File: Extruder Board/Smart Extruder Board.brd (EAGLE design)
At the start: 36 x 30 mm, 17 parts

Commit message: BCN3D Electronics REV.E tested and manufactured
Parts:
- removed FFC1: FFC_20V_90G_1MM", MarcEagleParts:SAMTEC_ZF1-T-WT
- removed HALL: (no value), adafruit:JSTPH3
- removed HOTEND: (no value), MarcEagleParts:JSTPH3
- removed TP1, TP2, TP3, TP4, TP7: TPB1,27, testpad:B1,27
- added CN1: (no value), MarcEagleParts:JST_PA_04
- added ENDSTOP: (no value), SparkFun-Connectors:JST-2-SMD
- added U$6: (no value), MarcEagleParts:FCIM_LOGO
- added VERT_FFC1: FFC_20V_90G_1MM3, MarcEagleParts:FCI_20WAY_1MM_3ST
- moved U$3 25.0 mm to (1.50, 24.5)
- moved TP6 24.0 mm to (30.8, 23.9), flipped to the top, turned to 270 degrees
- moved TP5 12.3 mm to (7.01, 18.9), flipped to the top
- moved U$4 9.77 mm to (22.1, 4.47)
- moved U$2 5.71 mm to (24.0, 3.00)
- moved U$5 4.88 mm to (7.72, 6.78)
- moved U$1 4.67 mm to (31.0, 28.0)
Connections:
- removed net ATLVL: FFC1.20, HALL.2, TP4.TP
- new net GNDTHERM: CN1.4, VERT_FFC1.2
- new net Z-ENDSTOP: ENDSTOP.2, VERT_FFC1.20
- net +24V: now also CN1.1, VERT_FFC1.10, VERT_FFC1.12, VERT_FFC1.18, VERT_FFC1.19, VERT_FFC1.8; no longer FFC1.10, FFC1.12, FFC1.18, FFC1.19, FFC1.8, HOTEND.1
- net +5V: now also VERT_FFC1.1; no longer FFC1.1, HALL.3
- net GND: now also ENDSTOP.1, VERT_FFC1.11, VERT_FFC1.17, VERT_FFC1.4, VERT_FFC1.7, VERT_FFC1.9, VERT_FFC1.GND1, VERT_FFC1.GND2; no longer FFC1.11, FFC1.17, FFC1.2, FFC1.4, FFC1.7, FFC1.9, FFC1.GND1, FFC1.GND2, HALL.1, HOTEND.4, TP7.TP
- net HOTEND: now also CN1.2, VERT_FFC1.13, VERT_FFC1.14, VERT_FFC1.15, VERT_FFC1.16; no longer FFC1.13, FFC1.14, FFC1.15, FFC1.16, HOTEND.2, TP3.TP
- net HOTEND_THERM: now also CN1.3, VERT_FFC1.3; no longer FFC1.3, HOTEND.3, TP1.TP
- net LFAN: now also VERT_FFC1.5, VERT_FFC1.6; no longer FFC1.5, FFC1.6, TP2.TP
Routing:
- net Z-ENDSTOP: track 0.00 -> 43.1 mm
- net +5V: track 38.1 -> 4.72 mm, vias 1 -> 0
- net ATLVL: track 23.1 -> 0.00 mm, vias 2 -> 0
- net GNDTHERM: track 0.00 -> 22.5 mm
- net +24V: track 25.4 -> 8.94 mm, vias 1 -> 0
- net HOTEND_THERM: track 16.4 -> 19.7 mm, vias 2 -> 0
- net HOTEND: track 2.40 -> 0.00 mm, vias 1 -> 8
- net LFAN: track 30.5 -> 32.5 mm
- added copper zone on layer 16, net HOTEND
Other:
- board size 36 x 30 mm -> 33 x 30 mm
- board text added: "+"
- board text added: "BCN3D Electronics Extruder Board v1.0 Designed in Barcelona ___________________ May 2015 - REV_D"
- board text added: "HOTEND"
- board text added: "THRM"
- board text removed: "BCN3D Electronics çextruder Board v1.0 Designed in Barcelona ___________________ Extruder Board - Jan 2015 Marc Cobler - REV_B ___________________"
- board text removed: "Fundacio CIM"

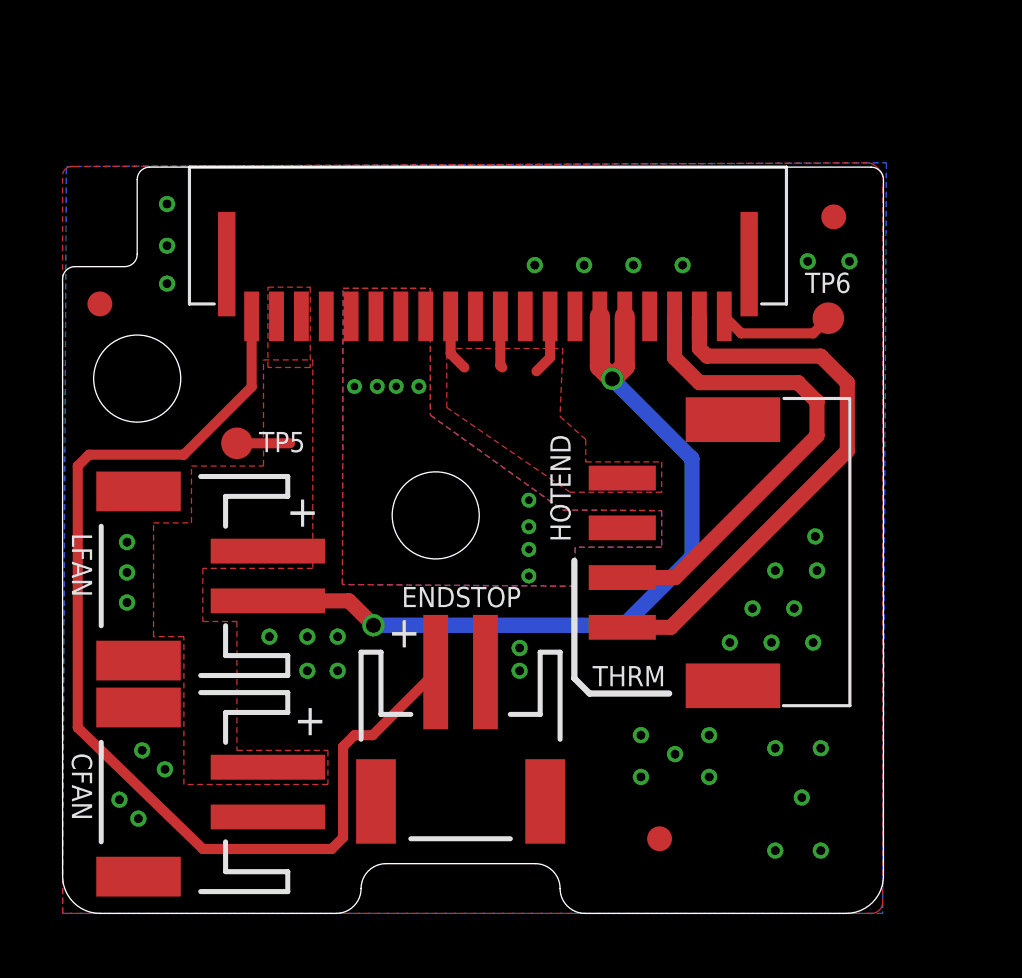
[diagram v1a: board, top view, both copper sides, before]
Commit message: File for the REV.H
Files from the REV.H Released with new and more documentation.
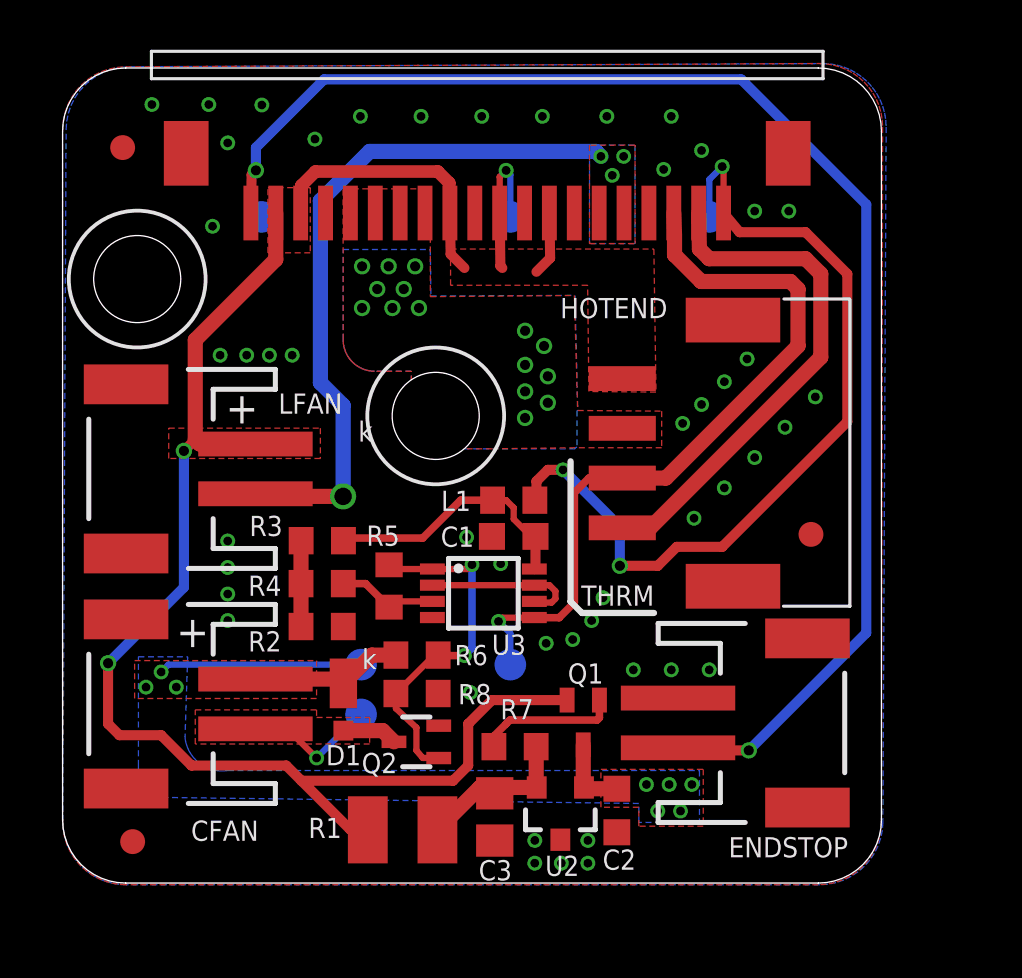
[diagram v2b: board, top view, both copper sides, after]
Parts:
- removed TP5, TP6: TPB1,27, testpad:B1,27
- removed U$4: (no value), MarcEagleParts:CC_LOGO
- added 24V, 5V, CFAN+, CFAN-, GND, THERM: TPB1,27, testpad:B1,27
- added C1, C2: 100n, rcl:C0603K
- added C3: 330n, rcl:C0805
- added D1: PD3S160, diode:POWERDI323
- added L1, R4, R6: 1k, rcl:R0603
- added Q1: BC807W, transistor-pnp:SOT323-BEC
- added Q2: MOSFET-NSOT323, MarcEagleParts:SOT323
- added R1: 100, rcl:R1210
- added R2, R8: 10k, rcl:R0603
- added R3: 5k23, rcl:R0603
- added R5: 200k, rcl:R0603
- added R7: 22.6K, rcl:R0603
- added U2: LM3480IM4, SparkFun-PowerIC:SOT23-3
- added U3: LM392MMSOP8, MarcEagleParts:MSOP8
- VERT_FFC1: value FFC_20V_90G_1MM3 -> 68612014422; device MarcEagleParts:FCI_20WAY_1MM_3ST -> FPC_FFC_Connectors_:68612014422
- moved U$6 22.8 mm to (30.9, -0.50)
- moved U$2 21.2 mm to (2.82, 2.89)
- moved U$1 12.8 mm to (30.1, 15.2)
- moved U$5 12.6 mm to (8.01, 19.4)
- moved ENDSTOP 12.6 mm to (28.4, 7.66), turned to 270 degrees
- moved VERT_FFC1 6.88 mm to (10.8, 29.3)
- moved U$3 6.35 mm to (2.41, 30.8)
- moved LFAN 4.33 mm to (4.05, 17.9)
- moved CN1 4.00 mm to (25.0, 18.5)
- moved CFAN 3.58 mm to (4.05, 8.42)
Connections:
- new net 12V: C2.2, CFAN+.TP, CFAN.2, D1.C, Q1.3, R6.2, U2.1
- new net DRAIN: CFAN-.TP, CFAN.1, D1.A, Q2.3
- new net IN: C3.2, R1.2, R7.1, U2.2
- new net N$1: Q1.1, R7.2
- new net N$2: C1.1, L1.2, R3.2, U3.8
- new net N$3: U3.2, U3.6, U3.7
- new net N$4: R2.2, R3.1, R4.2
- new net N$5: R4.1, R5.2, U3.3
- new net OUT: Q2.1, R5.1, R6.1, R8.2, U3.1
- net +24V: now also 24V.TP, Q1.2, R1.1; no longer CFAN.2, TP5.TP
- net +5V: now also 5V.TP, L1.1; no longer TP6.TP
- net GND: now also C1.2, C2.1, C3.1, GND.TP, Q2.2, R2.1, R8.1, U2.3, U3.4; no longer CFAN.1, VERT_FFC1.GND1, VERT_FFC1.GND2
- net HOTEND_THERM: now also THERM.TP, U3.5
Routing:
- net +24V: track 8.94 -> 71.5 mm, vias 0 -> 3
- net +5V: track 4.72 -> 34.5 mm, vias 0 -> 3
- net 12V: track 0.00 -> 17.5 mm, vias 0 -> 8
- net OUT: track 0.00 -> 14.4 mm, vias 0 -> 2
- net Z-ENDSTOP: track 43.1 -> 57.2 mm, vias 0 -> 2
- net N$2: track 0.00 -> 11.1 mm
- net HOTEND_THERM: track 19.7 -> 30.7 mm, vias 0 -> 1
- net DRAIN: track 0.00 -> 7.68 mm, vias 0 -> 1
- net IN: track 0.00 -> 6.56 mm
- net N$3: track 0.00 -> 6.34 mm
- net N$1: track 0.00 -> 5.68 mm
- net LFAN: track 32.5 -> 28.0 mm, vias 2 -> 4
- net N$5: track 0.00 -> 4.20 mm
- net N$4: track 0.00 -> 3.45 mm
- net GNDTHERM: track 22.5 -> 20.9 mm
- added copper zone on layer 1, net 12V
- added copper zone on layer 16, net 12V
- added copper zone on layer 1, net DRAIN
- added copper zone on layer 1, net LFAN
- added copper zone on layer 16, net LFAN
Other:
- board size 33 x 30 mm -> 32.9 x 32.8 mm
- board text added: "BCN3D Electronics Extruder Board Designed in Barcelona ___________________ JAN 2017 - REV_H"
- board text added: "k"
- board text removed: "BCN3D Electronics Extruder Board v1.0 Designed in Barcelona ___________________ May 2015 - REV_D"
